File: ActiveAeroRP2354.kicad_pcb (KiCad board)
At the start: 6 copper layers, 30 x 75 mm, 150 parts, among them J1 TGCNT, J10 UART1_RAD, J11 SPI, J12 UART3, J13 RUNCAM, J14 Conn_01x06_MountingPin, J15 Conn_01x03_MountingPin, J2 I2C, J3 SRV1, J4 USB_C_Receptacle_USB2.0_16P, J5 UFL, J6 ARM, J7 SRV2, J8 SRV4, J9 SRV3, Q1 SiA449DJ, Q2 AO3401A, Q3 AO3401A, SW1 SW_Push, SW2 SW_Push, U1 LSM6DSV320, U10 AP7347DQ-33W5-7, U11 MCP2562-E-MF, U12 MMC5983MA, U13 STM32H747XIHx, U18 AP63205WU, U2 WE-TVS-82400102, U3 MIA-M10Q, U4 W25N512GV, U5 MS5611-01BA, U6 SCH16T, U7 BMI563, U8 INA238, U9 APS6404L-3SQRx-SN, Y1 ECS-.327-6-1210-TR, Y2 32.768khz, Y3 25Mhz

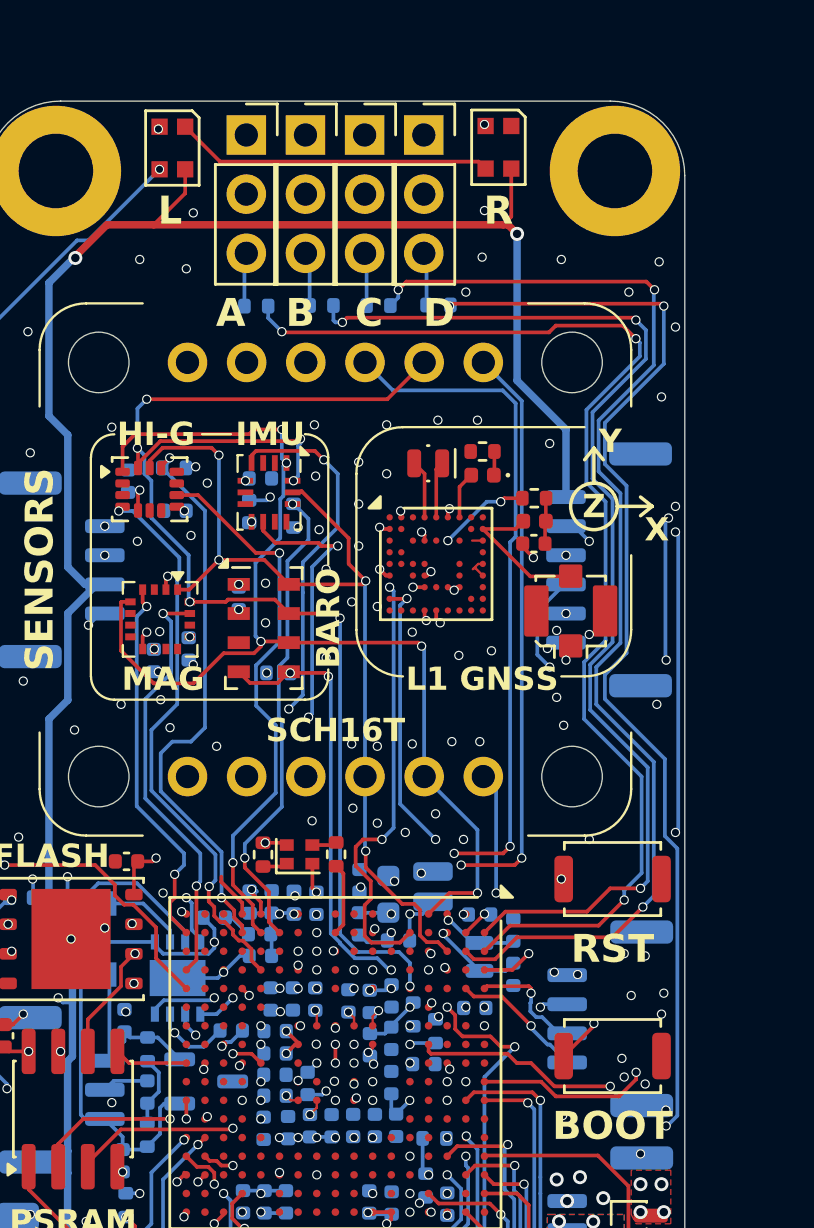
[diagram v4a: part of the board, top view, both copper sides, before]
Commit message: finished silks
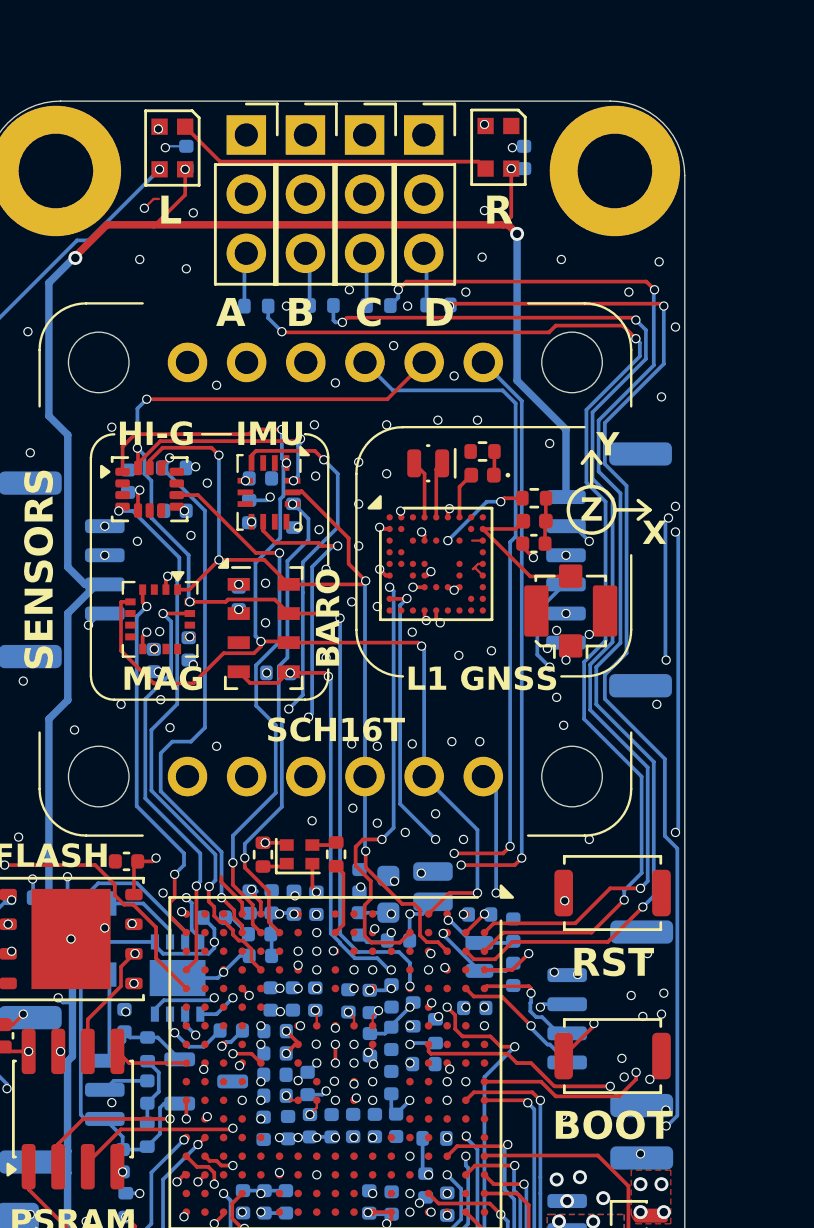
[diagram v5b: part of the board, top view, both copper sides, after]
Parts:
- added C65: 100nF, Capacitor_SMD:C_0402_1005Metric, B.Cu at (38.6, 27.4)
- added C66: 100nF, Capacitor_SMD:C_0402_1005Metric, B.Cu at (53.1, 27.4)
- moved SW2 0.60 mm to (56.9, 59.0)
- moved REF** 0.18 mm to (56.0, 42.5)
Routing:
- net GND: track 51.2 -> 53.0 mm, vias 200 -> 210
- net +5V: track 122.1 -> 122.8 mm, vias 4 -> 6
